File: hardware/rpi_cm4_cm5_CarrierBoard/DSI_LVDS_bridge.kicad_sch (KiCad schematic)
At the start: 28 parts, among them Q10 SSM3K56FS,LF, Q11 SSM3K56FS,LF, U15 SN65DSI84ZXHR, U16 SN74LVC1G125DBVR

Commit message: Added power input protection & filter Added dedicated QWIIC connector on RPI CMx I2C6 bus Adjusted power table and PinMux Updated schematics accordingly
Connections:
- net SYS_~{RST} renamed DSI_BRDG_~{RST}
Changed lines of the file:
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@@
 		)
 	)
-	(hierarchical_label "SYS_~{RST}"
+	(hierarchical_label "DSI_BRDG_~{RST}"
 		(shape input)
 		(at 38.1 113.03 180)

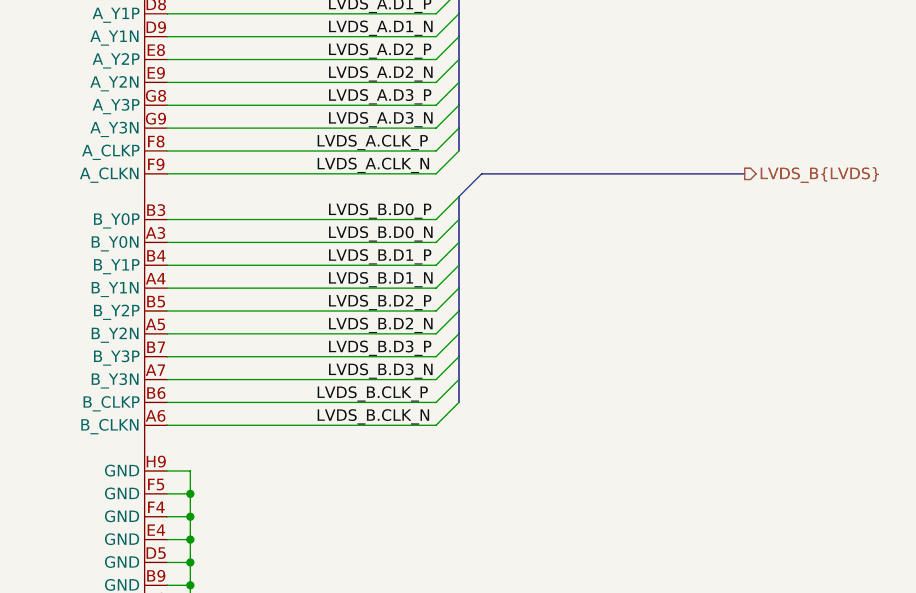
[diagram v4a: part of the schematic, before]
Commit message: Update schematics based on PCB preliminary placement Add preliminary design rules to PCB
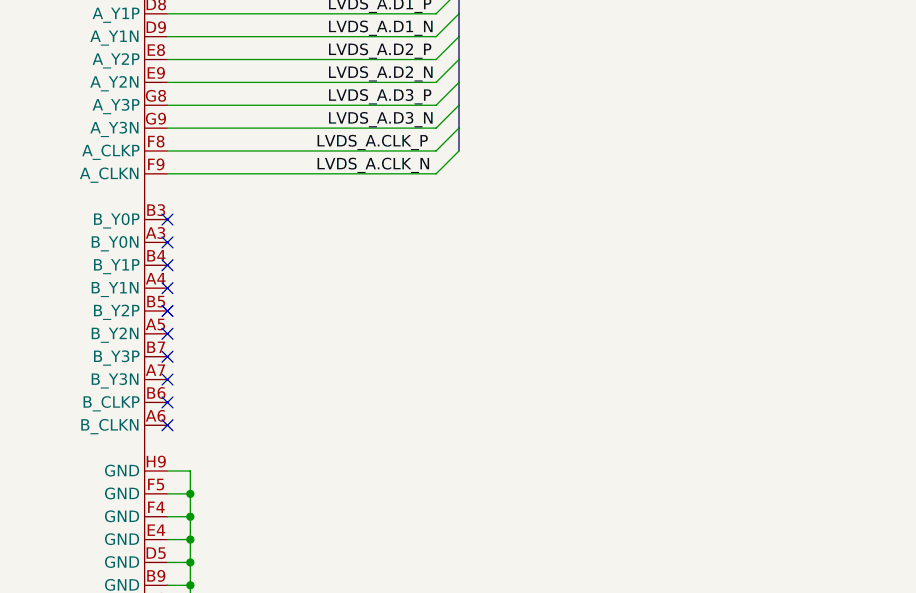
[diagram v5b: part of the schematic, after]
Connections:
- net LVDS_B.CLK_N: no longer names the net of U15.A6 (B_CLKN)
- net LVDS_B.CLK_P: no longer names the net of U15.B6 (B_CLKP)
- net LVDS_B.D0_N: no longer names the net of U15.A3 (B_Y0N)
- net LVDS_B.D0_P: no longer names the net of U15.B3 (B_Y0P)
- net LVDS_B.D1_N: no longer names the net of U15.A4 (B_Y1N)
- net LVDS_B.D1_P: no longer names the net of U15.B4 (B_Y1P)
- net LVDS_B.D2_N: no longer names the net of U15.A5 (B_Y2N)
- net LVDS_B.D2_P: no longer names the net of U15.B5 (B_Y2P)
- net LVDS_B.D3_N: no longer names the net of U15.A7 (B_Y3N)
- net LVDS_B.D3_P: no longer names the net of U15.B7 (B_Y3P)
- no-connect marks 2 -> 12

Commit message: Update PCB design rules for outer layers differential pairs Update preliminary component placement Update schematics based on PCB placement & remove duplicata / unnecessary components Update design notes and power table
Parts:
- removed C84, C85, C86: 0.1u, footprint:CAP_NONPOL_0402, symbol KicadCompDb:Capacitors/CAP_CER_SMT_00001
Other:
- moved on the sheet: C80, C81, C82, C83
